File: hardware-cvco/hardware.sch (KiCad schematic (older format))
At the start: 161 parts, among them J1 SMA, J2 SMA, J3 SMA, J4 SMA, J5 SMA, J6 SMA, J7 SMA, J8 Pickit 2, J9 DC, Q1 AOD403, Q2 MBT2222, SW1 On/Off, U1 74LS07, U10 TPS61046, U11 BQ21040, U12 LM324, U13 LM317DCYR, U14 LM386, U2 NLB-310-T1, U3 NLB-310-T1, U4 NLB-310-T1, U5 NLB-310-T1, U6 PIC12F675-ISN, U7 NLB-310-T1, U8 NLB-310-T1, U9 NLB-310-T1, Y1 CVCO55CW-0100-0200, Y2 CVCO55CW-0200-0500, Y3 CV55CW500-1000, Y4 CVCO55CW-1000-2000, Y5 CV55BE1600-3200, Y6 CVCO55CC-3180-3710, Y7 CVCO55CW-3500-4500

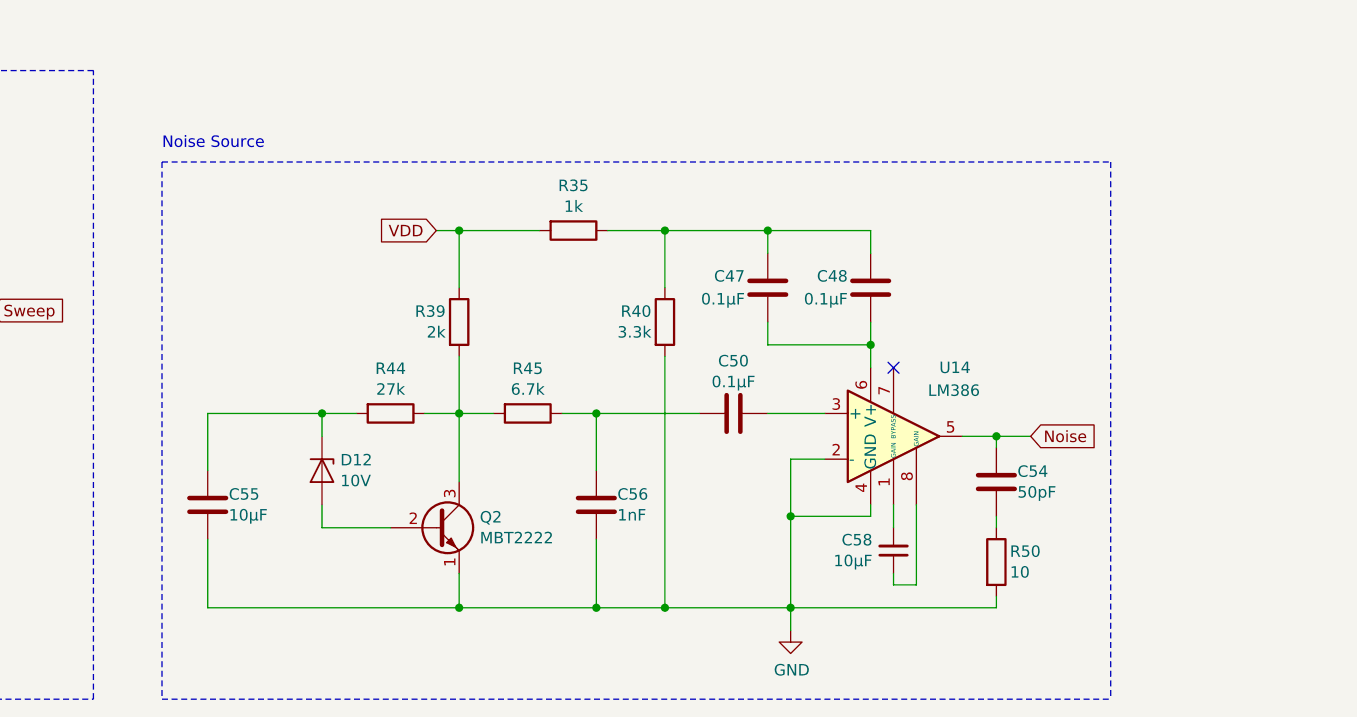
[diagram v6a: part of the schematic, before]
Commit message: Noise Source routing - CVCO.
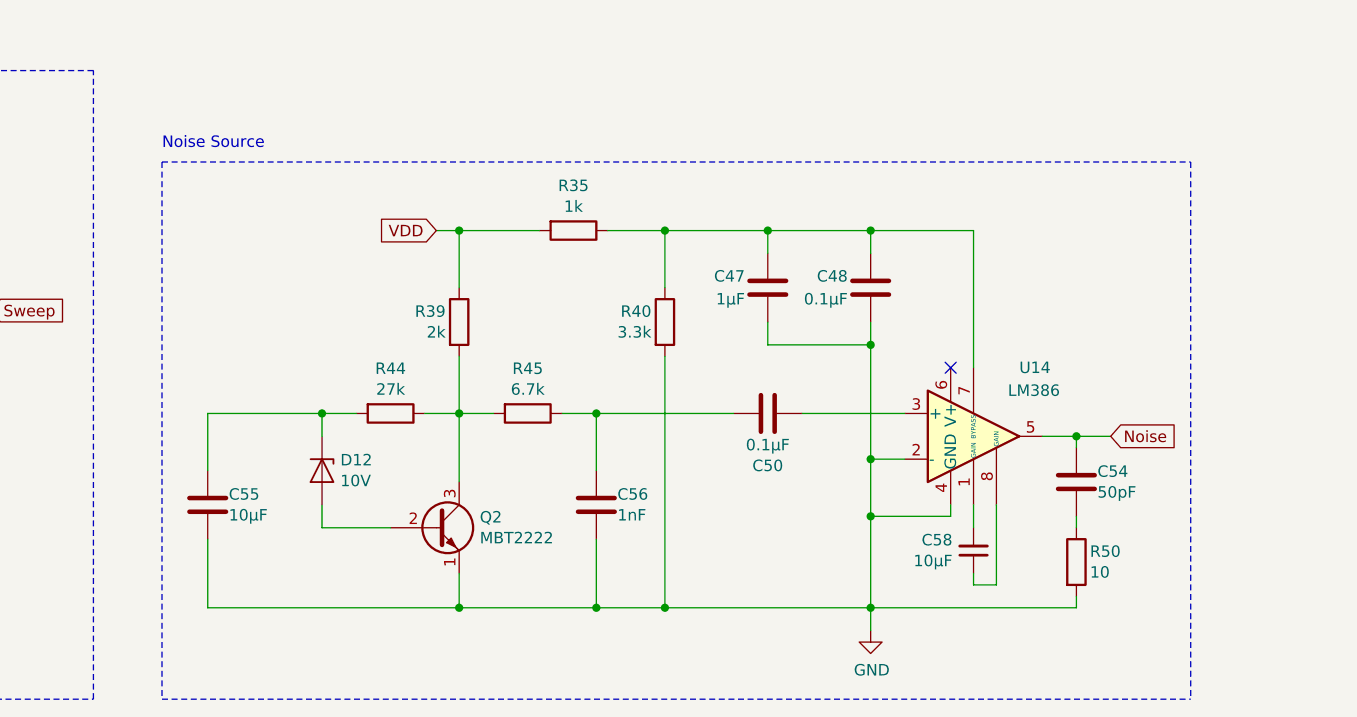
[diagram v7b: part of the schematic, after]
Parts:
- C47: value 0.1μF -> 1μF
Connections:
- net GND: now also C47.1, C48.1
- net at U14.3 (+): now also C50.2; no longer C50.1
- net at U14.7 (BYPASS): now also C47.2, C48.2, R35.1, R40.1
- net at C56.2, R45.1: now also C50.1; no longer C50.2
- now unconnected: U14.6 (V+)
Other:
- moved on the sheet: C50, C54, C58, R50, U14
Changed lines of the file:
@@
 	19600 4900 22600 4900
 Wire Wire Line
-	19050 12750 18900 12750
-Text GLabel 19950 12650 2    50   Input ~ 0
+	19400 12750 19250 12750
+Text GLabel 20300 12650 2    50   Input ~ 0
 Noise
-NoConn ~ 19350 12350
-Wire Wire Line
-	18900 13500 18900 13400
+NoConn ~ 19600 12350
+Wire Wire Line
+	19250 13500 19250 13400
 $Comp
 L power:GND #PWR058
 U 1 1 6A56C646
-P 18900 13500
-F 0 "#PWR058" H 18900 13250 50  0001 C CNN
-F 1 "GND" H 18905 13327 50  0000 C CNN
-F 2 "" H 18900 13500 50  0001 C CNN
-F 3 "" H 18900 13500 50  0001 C CNN
-	1    18900 13500
-	1    0    0    -1
-$EndComp
-Wire Wire Line
-	18900 12750 18900 13000
-Wire Wire Line
-	19450 12950 19450 13300
-Wire Wire Line
-	19450 13300 19350 13300
-Wire Wire Line
-	19350 13300 19350 13250
-Wire Wire Line
-	19350 12950 19350 13050
+P 19250 13500
+F 0 "#PWR058" H 19250 13250 50  0001 C CNN
+F 1 "GND" H 19255 13327 50  0000 C CNN
+F 2 "" H 19250 13500 50  0001 C CNN
+F 3 "" H 19250 13500 50  0001 C CNN
+	1    19250 13500
+	1    0    0    -1
+$EndComp
+Wire Wire Line
+	19250 12750 19250 13000
+Wire Wire Line
+	19800 12950 19800 13300
+Wire Wire Line
+	19800 13300 19700 13300
+Wire Wire Line
+	19700 13300 19700 13250
+Wire Wire Line
+	19700 12950 19700 13050
 $Comp
 L Device:C_Small C58
 U 1 1 6B808B12
-P 19350 13150
-F 0 "C58" H 19258 13104 50  0000 R CNN
-F 1 "10μF" H 19258 13195 50  0000 R CNN
-F 2 "Capacitor_SMD:C_0805_2012Metric_Pad1.15x1.40mm_HandSolder" H 19350 13150 50  0001 C CNN
-F 3 "~" H 19350 13150 50  0001 C CNN
-	1    19350 13150
+P 19700 13150
+F 0 "C58" H 19608 13104 50  0000 R CNN
+F 1 "10μF" H 19608 13195 50  0000 R CNN
+F 2 "Capacitor_SMD:C_0805_2012Metric_Pad1.15x1.40mm_HandSolder" H 19700 13150 50  0001 C CNN
+F 3 "~" H 19700 13150 50  0001 C CNN
+	1    19700 13150
 	1    0    0    1
 $EndComp
 Wire Wire Line
-	19250 12950 19250 13000
-Wire Wire Line
-	19250 13000 18900 13000
-Wire Wire Line
-	18900 13000 18900 13400
-Wire Wire Line
-	19650 12650 19800 12650
-Connection ~ 19800 12650
-Wire Wire Line
-	19800 12650 19950 12650
-Connection ~ 18900 13400
-Wire Wire Line
-	18900 13400 19800 13400
+	19600 12950 19600 13000
+Wire Wire Line
+	19600 13000 19250 13000
+Wire Wire Line
+	19250 13000 19250 13400
+Wire Wire Line
+	20000 12650 20150 12650
+Connection ~ 20150 12650
+Wire Wire Line
+	20150 12650 20300 12650
+Connection ~ 19250 13400
+Wire Wire Line
+	19250 13400 20150 13400
 $Comp
 L Device:C C50
 U 1 1 6C06AB6A
-P 18650 12550
-F 0 "C50" V 18421 12550 50  0000 C CNN
-F 1 "0.1μF" V 18512 12550 50  0000 C CNN
-F 2 "Capacitor_SMD:C_0805_2012Metric_Pad1.15x1.40mm_HandSolder" H 18650 12550 50  0001 C CNN
-F 3 "~" H 18650 12550 50  0001 C CNN
-	1    18650 12550
-	0    1    1    0
+P 18800 12550
+F 0 "C50" V 18571 12550 50  0000 C CNN
+F 1 "0.1μF" V 18662 12550 50  0000 C CNN
+F 2 "Capacitor_SMD:C_0805_2012Metric_Pad1.15x1.40mm_HandSolder" H 18800 12550 50  0001 C CNN
+F 3 "~" H 18800 12550 50  0001 C CNN
+	1    18800 12550
+	0    -1   -1   0
 $EndComp
 $Comp
@@
 P 18800 12000
 F 0 "C47" H 18700 11950 50  0000 R CNN
-F 1 "0.1μF" H 18700 12050 50  0000 R CNN
+F 1 "1μF" H 18700 12050 50  0000 R CNN
 F 2 "Capacitor_SMD:C_0805_2012Metric_Pad1.15x1.40mm_HandSolder" H 18800 12000 50  0001 C CNN
 F 3 "~" H 18800 12000 50  0001 C CNN
@@
 VDD
 Wire Wire Line
-	18800 12550 19050 12550
-Wire Wire Line
 	17900 12550 18050 12550
 Connection ~ 18050 12550
-Wire Wire Line
-	18050 12550 18500 12550
 Wire Wire Line
 	18050 12550 18050 12800
@@
 	18800 12150 18800 12250
 Wire Wire Line
-	19250 12250 19250 12350
-Connection ~ 19250 12250
-Wire Wire Line
-	18350 12300 18350 13400
-Connection ~ 18350 13400
-Wire Wire Line
-	18350 13400 18900 13400
+	19250 12250 19250 12750
+Wire Wire Line
+	18350 13400 19250 13400
 Wire Wire Line
 	17450 12000 17450 11750
@@
 L Device:C C54
 U 1 1 6B999272
-P 19800 12850
-F 0 "C54" H 19892 12896 50  0000 L CNN
-F 1 "50pF" H 19892 12805 50  0000 L CNN
-F 2 "Capacitor_SMD:C_0805_2012Metric_Pad1.15x1.40mm_HandSolder" H 19800 12850 50  0001 C CNN
-F 3 "~" H 19800 12850 50  0001 C CNN
-	1    19800 12850
-	1    0    0    -1
-$EndComp
-Wire Wire Line
-	19800 13050 19800 13000
+P 20150 12850
+F 0 "C54" H 20242 12896 50  0000 L CNN
+F 1 "50pF" H 20242 12805 50  0000 L CNN
+F 2 "Capacitor_SMD:C_0805_2012Metric_Pad1.15x1.40mm_HandSolder" H 20150 12850 50  0001 C CNN
+F 3 "~" H 20150 12850 50  0001 C CNN
+	1    20150 12850
+	1    0    0    -1
+$EndComp
+Wire Wire Line
+	20150 13050 20150 13000
 $Comp
 L Device:R R50
 U 1 1 6A2553A3
-P 19800 13200
-F 0 "R50" H 19859 13246 50  0000 L CNN
-F 1 "10" H 19859 13155 50  0000 L CNN
-F 2 "Resistor_SMD:R_0805_2012Metric_Pad1.15x1.40mm_HandSolder" V 19730 13200 50  0001 C CNN
-F 3 "~" H 19800 13200 50  0001 C CNN
-	1    19800 13200
-	1    0    0    -1
-$EndComp
-Wire Wire Line
-	19800 13350 19800 13400
-Wire Wire Line
-	19800 12650 19800 12700
-Connection ~ 18900 13000
+P 20150 13200
+F 0 "R50" H 20209 13246 50  0000 L CNN
+F 1 "10" H 20209 13155 50  0000 L CNN
+F 2 "Resistor_SMD:R_0805_2012Metric_Pad1.15x1.40mm_HandSolder" V 20080 13200 50  0001 C CNN
+F 3 "~" H 20150 13200 50  0001 C CNN
+	1    20150 13200
+	1    0    0    -1
+$EndComp
+Wire Wire Line
+	20150 13350 20150 13400
+Wire Wire Line
+	20150 12650 20150 12700
+Connection ~ 19250 13000
 Wire Wire Line
 	17950 7400 17650 7400
@@
 	17950 7400 17950 8050
 Wire Notes Line
-	16150 11450 20300 11450
+	16150 11450 20650 11450
 Wire Notes Line
-	16150 13800 20300 13800
+	16150 13800 20650 13800
 Wire Notes Line
-	20300 11450 20300 13800
+	20650 11450 20650 13800
 $Comp
 L Amplifier_Audio:LM386 U14
 U 1 1 6798D2B2
-P 19350 12650
-F 0 "U14" H 19550 12950 50  0000 L CNN
-F 1 "LM386" H 19500 12850 50  0000 L CNN
-F 2 "Package_SO:SO-8_5.3x6.2mm_P1.27mm" H 19450 12750 50  0001 C CNN
-F 3 "http://www.ti.com/lit/ds/symlink/lm386.pdf" H 19550 12850 50  0001 C CNN
-	1    19350 12650
-	1    0    0    -1
-$EndComp
+P 19700 12650
+F 0 "U14" H 19900 12950 50  0000 L CNN
+F 1 "LM386" H 19850 12850 50  0000 L CNN
+F 2 "Package_SO:SO-8_5.3x6.2mm_P1.27mm" H 19800 12750 50  0001 C CNN
+F 3 "http://www.ti.com/lit/ds/symlink/lm386.pdf" H 19900 12850 50  0001 C CNN
+	1    19700 12650
+	1    0    0    -1
+$EndComp
+Connection ~ 19250 12250
+Connection ~ 19250 12750
+Wire Wire Line
+	19700 12350 19700 11750
+Wire Wire Line
+	19700 11750 19250 11750
+Connection ~ 19250 11750
+Connection ~ 18350 13400
+Wire Wire Line
+	18050 12550 18650 12550
+Wire Wire Line
+	18950 12550 19400 12550
+Wire Wire Line
+	18350 12300 18350 13400
 $EndSCHEMATC

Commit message: PIC routing - CVCO.
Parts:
- removed J8: Pickit 2, Connector_PinSocket_2.54mm:PinSocket_1x06_P2.54mm_Vertical, symbol Connector_Generic:Conn_02x03_Counter_Clockwise
- added J8: Pickit 2, Connector_PinSocket_2.54mm:PinSocket_1x03_P2.54mm_Horizontal, symbol Connector_Generic:Conn_01x03
- C47: LCSC Part # (none) -> C116352
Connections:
- net DC: no longer C46.1, D8.2 (A), U11.6 (VIN)
- net GP0: now also J8.2 (Pin_2)
- net GP1: now also J8.3 (Pin_3)
- net GP3: now also J8.1 (Pin_1)
- net P2_VDD renamed Boost
- net Boost: no longer C23.1, C24.1, C25.1, C26.1, U1.14 (VCC), U6.1 (VDD)
- new net VDD: C23.1, C24.1, C25.1, C26.1, C46.1, D8.2 (A), U1.14 (VCC), U11.6 (VIN), U6.1 (VDD)
- no-connect marks 2 -> 1
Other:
- moved on the sheet: C44, C47, C48, C49, C50, C53, C54, C55, C56, C58, D12, Q2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
